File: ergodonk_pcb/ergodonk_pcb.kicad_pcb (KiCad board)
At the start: 2 copper layers, 184 x 152.6 mm, 118 parts, among them J1 AudioJack4, Q1 TIP120, SW00 SW_PUSH_LED, SW01 SW_PUSH_LED, SW02 SW_PUSH_LED, SW03 SW_PUSH_LED, SW04 SW_PUSH_LED, SW05 SW_PUSH_LED, SW06 SW_PUSH_LED, SW07 SW_PUSH_LED, SW10 SW_PUSH_LED, SW11 SW_PUSH_LED, SW12 SW_PUSH_LED, SW13 SW_PUSH_LED, SW14 SW_PUSH_LED, SW15 SW_PUSH_LED, SW16 SW_PUSH_LED, SW17 SW_PUSH_LED, SW20 SW_PUSH_LED, SW21 SW_PUSH_LED, SW22 SW_PUSH_LED, SW23 SW_PUSH_LED, SW24 SW_PUSH_LED, SW25 SW_PUSH_LED, SW26 SW_PUSH_LED, SW27 SW_PUSH_LED, SW30 SW_PUSH_LED, SW31 SW_PUSH_LED, SW32 SW_PUSH_LED, SW33 SW_PUSH_LED, SW34 SW_PUSH_LED, SW35 SW_PUSH_LED, SW36 SW_PUSH_LED, SW37 SW_PUSH_LED, SW40 SW_PUSH_LED, SW42 SW_PUSH_LED, SW43 SW_PUSH_LED, SW44 SW_PUSH_LED, SW45 SW_PUSH_LED, SW46 SW_PUSH_LED, SW47 SW_PUSH_LED, SW50 SW_PUSH_LED, SW51 SW_PUSH_LED, SW52 SW_PUSH_LED, SW53 SW_PUSH_LED, SW54 SW_PUSH_LED, SW55 SW_PUSH_LED, SW56 SW_PUSH_LED, SW57 SW_PUSH_LED, SW58 SW_PUSH_LED

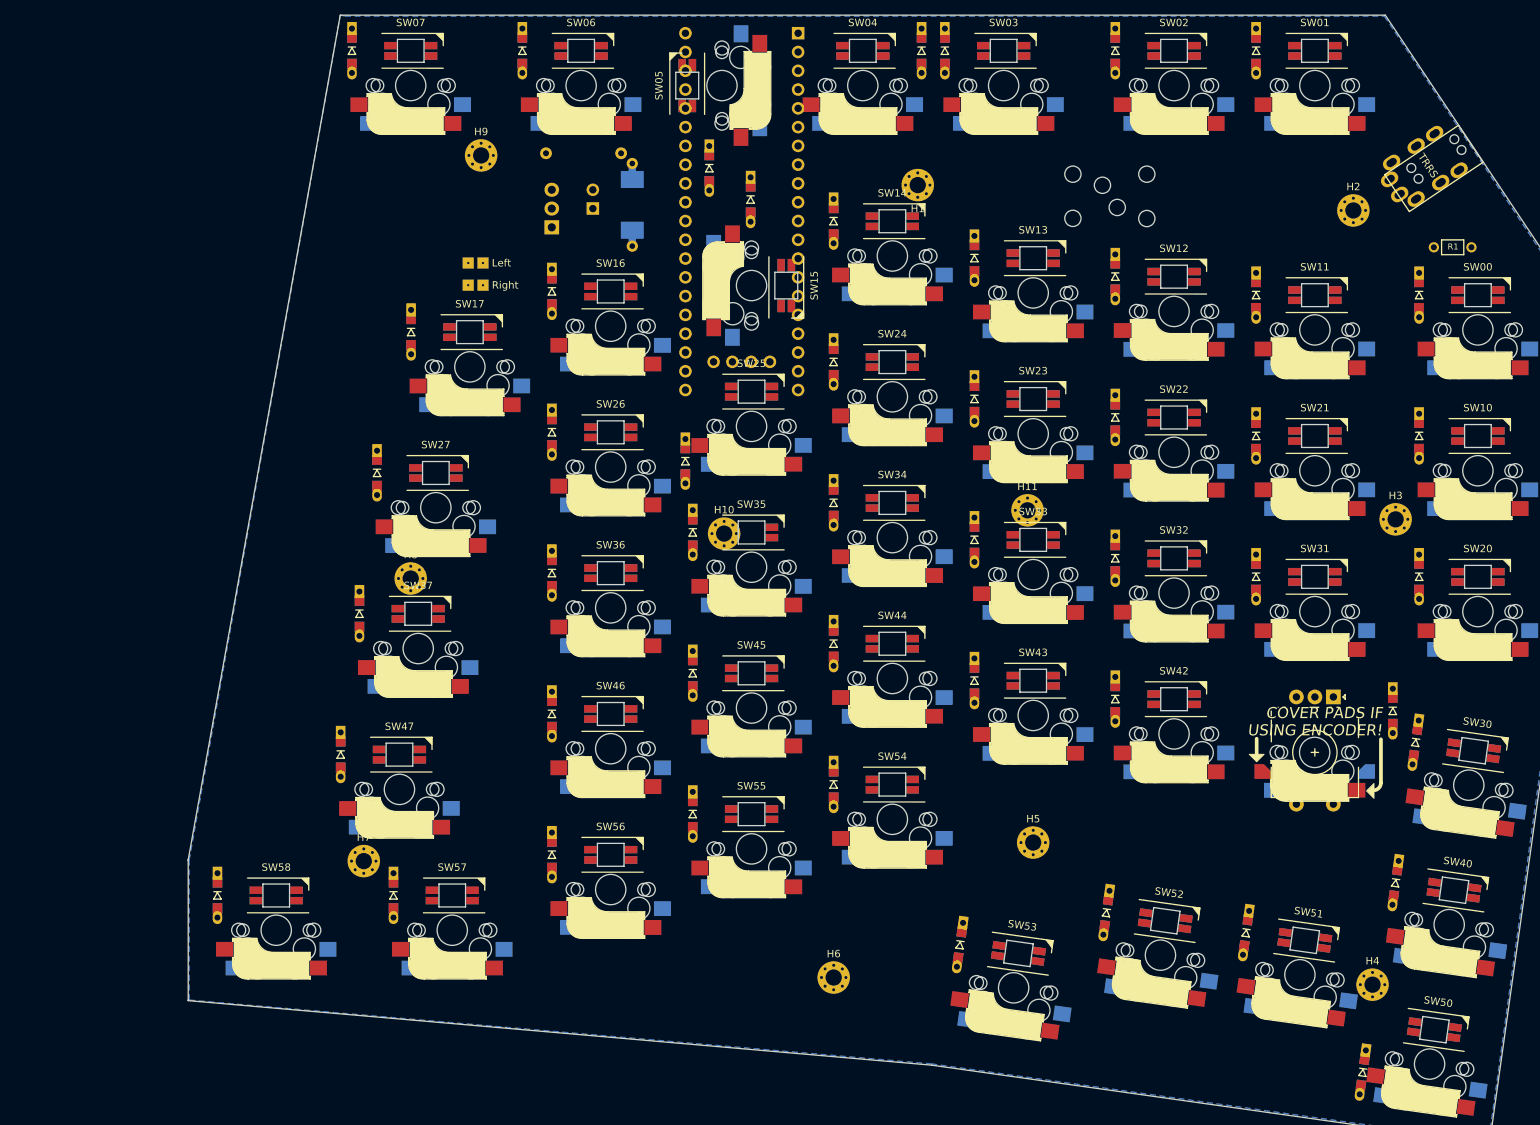
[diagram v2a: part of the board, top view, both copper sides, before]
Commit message: Right hand added Built new footprints for RH/LH combo keys Added jumpers for optional LEDs"
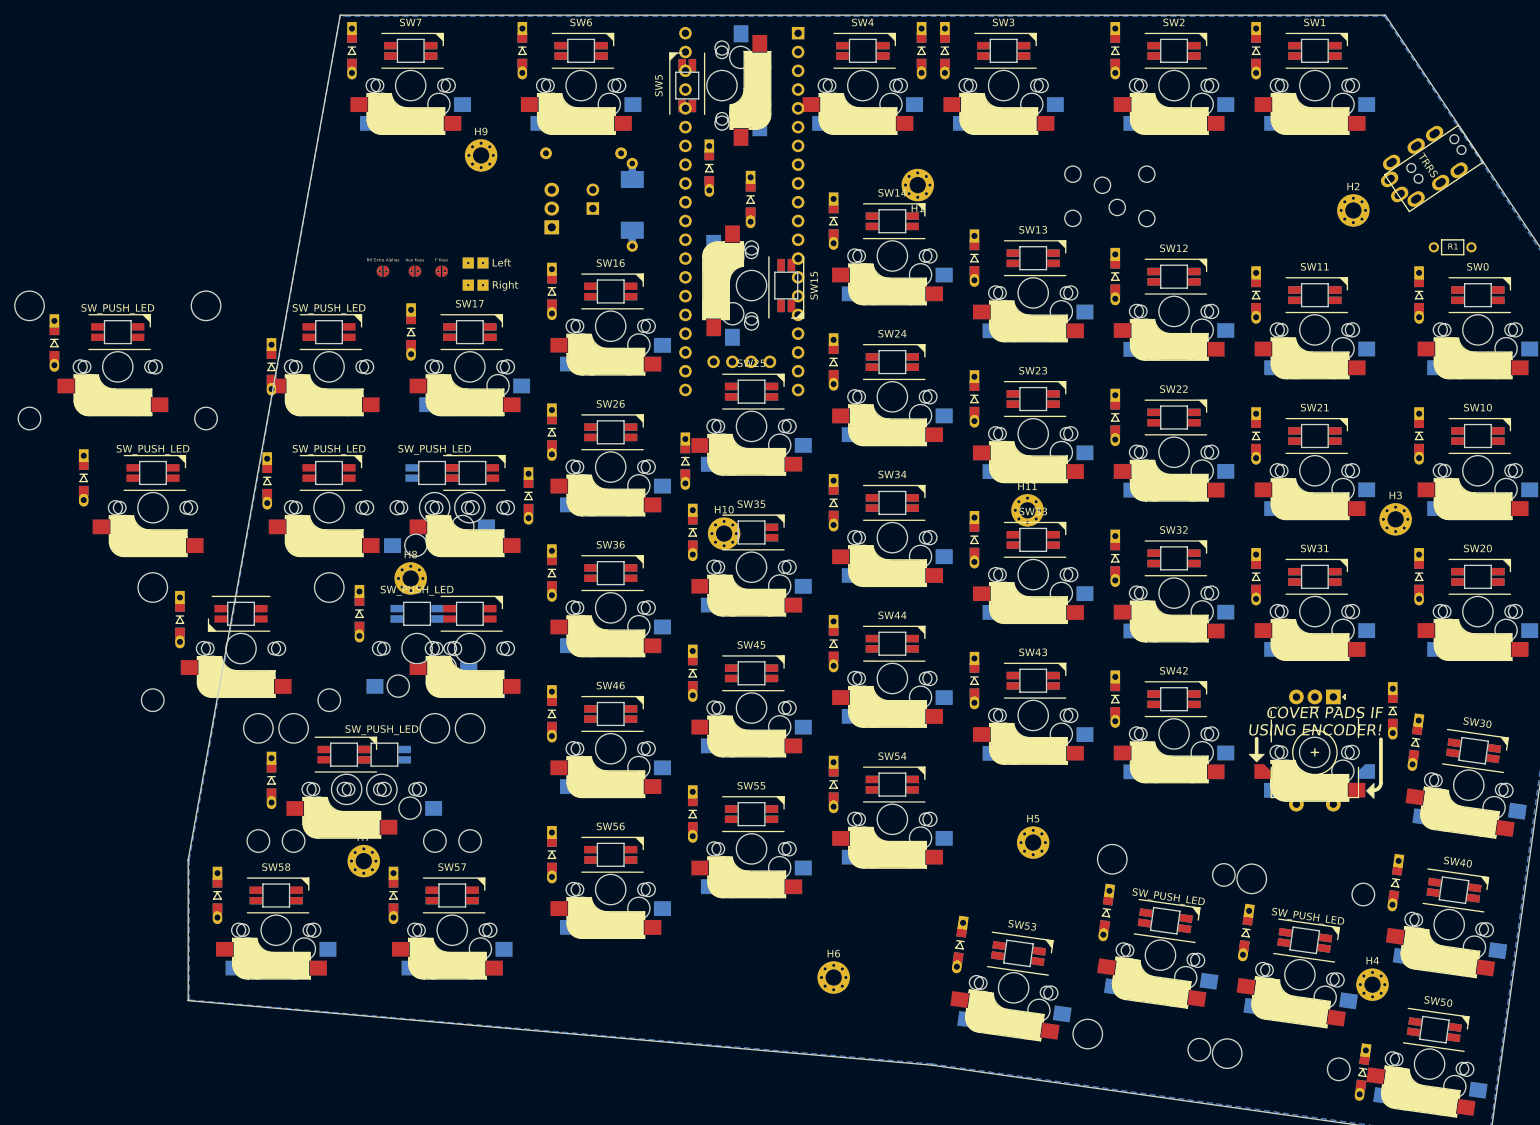
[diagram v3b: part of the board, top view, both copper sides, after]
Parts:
- added D08_RH10: D, ergodonk_kicad_library:D3_TH_SMD_v3_ergodonk, B.Cu at (0.95, 69.8)
- added D18_RH10: D, ergodonk_kicad_library:D3_TH_SMD_v3_ergodonk, F.Cu at (30.3, 73.0)
- added D28_RH10: D, ergodonk_kicad_library:D3_TH_SMD_v3_ergodonk, B.Cu at (4.92, 88.0)
- added D38_RH10: D, ergodonk_kicad_library:D3_TH_SMD_v3_ergodonk, F.Cu at (29.7, 88.4)
- added D48_RH10: D, ergodonk_kicad_library:D3_TH_SMD_v3_ergodonk, F.Cu at (17.9, 107.2)
- added JP2: RH Extra Alphas, Keebio-Parts:solder_jumper, F.Cu at (45.4, 60.0)
- added JP4: Aux Keys, Keebio-Parts:solder_jumper, F.Cu at (49.7, 60.0)
- added JP5: F Keys, Keebio-Parts:solder_jumper, F.Cu at (53.3, 60.0)
- added SW08_RH10: SW_PUSH_LED, ergodonk_kicad_library:CherryMX_DoubleSided_Hotswap_miniE_2u_RH_ONLY, F.Cu at (9.53, 73.0)
- added SW18_RH10: SW_PUSH_LED, ergodonk_kicad_library:CherryMX_DoubleSided_Hotswap_miniE_1u_RH_ONLY, F.Cu at (38.1, 73.0)
- added SW28_RH10: SW_PUSH_LED, ergodonk_kicad_library:CherryMX_DoubleSided_Hotswap_miniE_1.5u_RH_ONLY, F.Cu at (14.3, 92.0)
- added SW38_RH10: SW_PUSH_LED, ergodonk_kicad_library:CherryMX_DoubleSided_Hotswap_miniE_1u_RH_ONLY, F.Cu at (38.1, 92.0)
- added SW48_RH10: SW_PUSH_LED, ergodonk_kicad_library:CherryMX_DoubleSided_Hotswap_miniE_2.25u_LH_ONLY, B.Cu at (26.2, 111.1)
- SW27: footprint ergodonk_kicad_library:CherryMX_DoubleSided_Hotswap_miniE -> ergodonk_kicad_library:CherryMX_DoubleSided_Hotswap_miniE_1.5u_LH_1u_RH
- SW37: footprint ergodonk_kicad_library:CherryMX_DoubleSided_Hotswap_miniE -> ergodonk_kicad_library:CherryMX_DoubleSided_Hotswap_miniE_1.75u_LH_1u_RH
- SW47: footprint ergodonk_kicad_library:CherryMX_DoubleSided_Hotswap_miniE -> ergodonk_kicad_library:CherryMX_DoubleSided_Hotswap_miniE_2.25u_LH_2.75u_RH
- SW51, SW52: footprint ergodonk_kicad_library:CherryMX_DoubleSided_Hotswap_miniE -> ergodonk_kicad_library:CherryMX_DoubleSided_Hotswap_miniE_2u_Vertical
- SW53: footprint ergodonk_kicad_library:CherryMX_DoubleSided_Hotswap_miniE -> ergodonk_kicad_library:CherryMX_DoubleSided_Hotswap_miniE_1.25u_Vertical
- SW57, SW58: footprint ergodonk_kicad_library:CherryMX_DoubleSided_Hotswap_miniE -> ergodonk_kicad_library:CherryMX_DoubleSided_Hotswap_miniE_1.25u
- moved D27 20.7 mm to (65.1, 90.4)
- moved D47 9.99 mm to (30.3, 128.9)
- moved SW47 2.38 mm to (45.2, 130.1)
- moved SW27 0.16 mm to (52.4, 92.0)
- moved SW37 0.16 mm to (50.0, 111.1)
- renumbered D00 to D0, D01 to D1, D02 to D2, D03 to D3, D04 to D4, D05 to D5, D06 to D6, D07 to D7, SW00 to SW0, SW01 to SW1, SW02 to SW2, SW03 to SW3, SW04 to SW4, SW05 to SW5, SW06 to SW6, SW07 to SW7
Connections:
- net col8 renamed col0
- SW0 pad 2: unconnected-(SW00-Pad2) -> Net-(SW0-Pad2)
- SW0 pad 4: unconnected-(SW00-Pad4) -> Net-(SW0-Pad4)
- SW1 pad 2: unconnected-(SW01-Pad2) -> Net-(SW2-Pad4)
- SW1 pad 4: unconnected-(SW01-Pad4) -> Net-(SW1-Pad4)
- SW10 pad 2: unconnected-(SW10-Pad2) -> Net-(SW0-Pad4)
- SW10 pad 4: unconnected-(SW10-Pad4) -> Net-(SW20-Pad2)
- SW2 pad 2: unconnected-(SW02-Pad2) -> Net-(SW3-Pad4)
- SW2 pad 4: unconnected-(SW02-Pad4) -> Net-(SW2-Pad4)
- SW20 pad 2: unconnected-(SW20-Pad2) -> Net-(SW20-Pad2)
- SW20 pad 4: unconnected-(SW20-Pad4) -> Net-(SW20-Pad4)
- SW3 pad 2: unconnected-(SW03-Pad2) -> Net-(SW3-Pad2)
- SW3 pad 4: unconnected-(SW03-Pad4) -> Net-(SW3-Pad4)
- SW30 pad 2: unconnected-(SW30-Pad2) -> Net-(JP4-Pad1)
- SW30 pad 4: unconnected-(SW30-Pad4) -> Net-(SW40-Pad2)
- SW4 pad 2: unconnected-(SW04-Pad2) -> Net-(SW5-Pad4)
- SW4 pad 4: unconnected-(SW04-Pad4) -> Net-(SW3-Pad2)
- SW40 pad 2: unconnected-(SW40-Pad2) -> Net-(SW40-Pad2)
- SW40 pad 4: unconnected-(SW40-Pad4) -> GND
- SW5 pad 2: unconnected-(SW05-Pad2) -> Net-(SW5-Pad2)
- SW5 pad 4: unconnected-(SW05-Pad4) -> Net-(SW5-Pad4)
- SW50 pad 2: unconnected-(SW50-Pad2) -> GND
- SW50 pad 4: unconnected-(SW50-Pad4) -> Net-(SW50-Pad4)
- SW51 pad 2: unconnected-(SW51-Pad2) -> Net-(SW50-Pad4)
- SW51 pad 4: unconnected-(SW51-Pad4) -> Net-(SW51-Pad4)
- SW52 pad 2: unconnected-(SW52-Pad2) -> Net-(SW51-Pad4)
- SW52 pad 4: unconnected-(SW52-Pad4) -> Net-(SW53-Pad2)
- SW53 pad 2: unconnected-(SW53-Pad2) -> Net-(SW53-Pad2)
- SW58 pad 2: unconnected-(SW58-Pad2) -> Net-(SW58-Pad2)
- SW6 pad 2: unconnected-(SW06-Pad2) -> Net-(SW6-Pad2)
- SW6 pad 4: unconnected-(SW06-Pad4) -> Net-(SW5-Pad2)
- SW7 pad 4: unconnected-(SW07-Pad4) -> Net-(SW6-Pad2)

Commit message: Added edgecuts with breakaway right hand
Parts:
- added U1: Elite-C-ZigZag, Keebio-Parts:Elite-C-ZigZag, F.Cu at (240.2, 51.2)
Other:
- board size 184 x 152.6 mm -> 216.6 x 156.7 mm

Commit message: Added speaker and cleaned up diode placement
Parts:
- added LS1: AST1109MLTRQ, ergodonk_kicad_library:AST1109MLTRQ, F.Cu at (57.9, 52.3)
- D0, D08_RH10, D1, D10, D11, D12, D13, D14, D16, D17, D2, D20, D21, D22, D23, D24, D25, D26, D27, D3, D30, D31, D32, D33, D34, D35, D36, D37, D40, D41, D42, D43, D44, D45, D46, D47, D50, D51, D52, D53, D54, D55, D56, D57, D58, D6, D7: moved to F.Cu
- D18_RH10, D48_RH10: moved to B.Cu
- moved U1 179.3 mm to (71.8, -10.1)
- moved D27 20.2 mm to (45.3, 86.3)
- moved D41 19.5 mm to (162.5, 119.4)
- moved D28_RH10 18.5 mm to (23.3, 86.3)
- moved D08_RH10 17.9 mm to (18.6, 72.8)
- moved D48_RH10 17.7 mm to (35.1, 111.2)
- moved D18_RH10 16.7 mm to (46.0, 67.3)
- moved D50 7.93 mm to (179.0, 160.5)
- moved H3 6.66 mm to (182.4, 86.9)
- moved H10 6.31 mm to (95.4, 90.5)
- moved D37 5.70 mm to (39.0, 111.1)
- moved H2 4.90 mm to (180.9, 54.3)
- moved H1 4.48 mm to (119.9, 44.4)
- moved H4 3.92 mm to (178.6, 152.7)
- moved D5 3.53 mm to (91.9, 48.7)
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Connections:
- ULH1 pad 27: unconnected-(ULH1-Pad27) -> SPEAKER
